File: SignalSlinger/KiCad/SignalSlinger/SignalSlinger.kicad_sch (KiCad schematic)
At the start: 58 parts, among them J101 Conn_01x02, J102 Conn_01x02, J103 Conn_01x02, J104 Conn_01x02, J105 Conn_01x02, J106 Conn_01x02, J107 DB9 Female, J108 Conn_01x02, J109 Conn_01x03, J110 Conn_01x02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

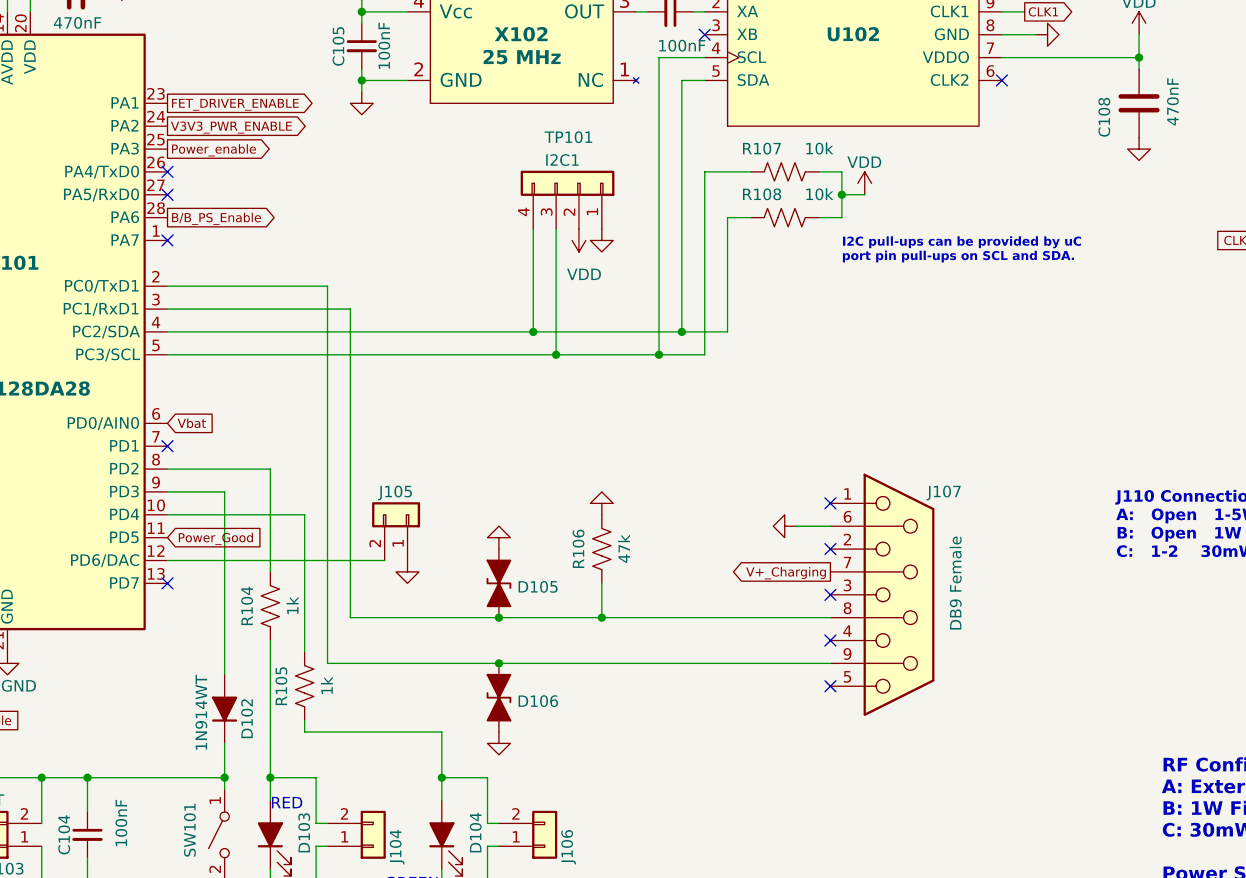
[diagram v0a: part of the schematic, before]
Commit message: KiCad
Added support for straight key and paddles
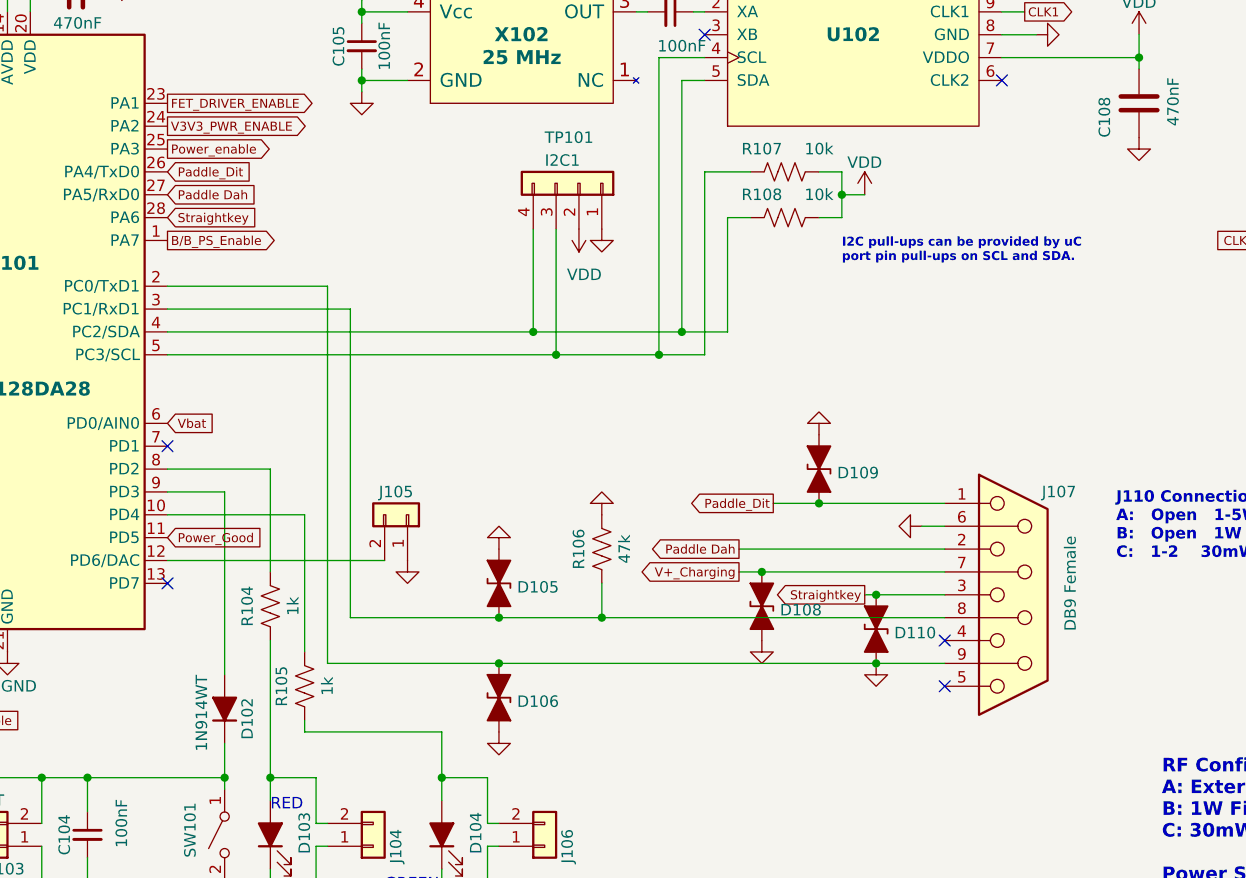
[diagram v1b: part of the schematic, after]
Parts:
- added D108, D109, D110: ESD9B5.0ST5G_1, Diode_SMD:D_0603_1608Metric, symbol Diode:ESD9B5.0ST5G_1
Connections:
- net B/B_PS_Enable: now also U101.1 (PA7); no longer U101.28 (PA6)
- net GND: now also D106.1 (A1), J107.9, U101.2 (PC0/TxD1), D108.2 (A2), D109.1 (A1), D110.2 (A2)
- net V+_Charging: now also D108.1 (A1)
- net Paddle_Dit: now reaches U101.26 (PA4/TxD0)
- net Paddle_Dit: now also J107.1, D109.2 (A2)
- net Paddle Dah: now reaches U101.27 (PA5/RxD0)
- net Paddle Dah: now also J107.2
- net Straightkey: now reaches J107.3
- net Straightkey: now also U101.28 (PA6), D110.1 (A1)
- no-connect marks 22 -> 16
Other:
- moved on the sheet: J107

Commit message: Updates
Schematic and PCB updates
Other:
- note removed: "J110 Connections A: Open 1-5W Variable RF Out CW Tx B: Open 1W Fixed RF Out CW Tx C: 1-2 30mW Fixed RF Out CW Tx"
- title: (none) -> SignalSlinger Design
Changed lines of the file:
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@@
 (kicad_sch (version 20211123) (generator eeschema)
   (paper "A4")
+  (title_block
+    (title "SignalSlinger Design")
+    (date "2023-06-20")
+    (rev "1.0")
+  )
   (junction (at 158.75 133.35) (diameter 0) (color 0 0 0 0)
   )
@@
     (effects (font (size 1.27 1.27) (thickness 0.254) bold) (justify left bottom))
   )
-  (text "J110 Connections\nA:   Open   1-5W Variable RF Out CW Tx\nB:   Open   1W Fixed RF Out CW Tx\nC:   1-2    30mW Fixed RF Out CW Tx"
-    (at 185.42 121.92 0)
-    (effects (font (size 1.27 1.27) (thickness 0.254) bold) (justify left bottom))
-  )
   (text "RF Configurations\nA: External 5-12.5V = 1-5W Variable RF Out CW Tx\nB: 1W Fixed RF Out CW Tx\nC: 30mW Fixed RF Out CW Tx\n\nPower Source Configurations\n1. External 5-12.5V\n2. Internal LiIon Battery (3.2-4.2V)\n\n"
     (at 190.5 165.1 0)
@@
       (reference "#PWR0233") (unit 1) (value "GND") (footprint "")
     )
+    (path "/b7c888bf-e50e-45b8-8886-9bc5abf637fe/7e7a61a5-2fd3-45c0-94ac-d31b757fdb9c"
+      (reference "#PWR0234") (unit 1) (value "GND") (footprint "")
+    )
     (path "/da189f43-fd1f-445a-980b-345fda8b9a74/b600cc7c-7732-4f3a-9659-2132a29c4d79"
       (reference "#PWR0301") (unit 1) (value "GND") (footprint "")
@@
       (reference "HDWR412") (unit 1) (value "Pin Header Shorting Jumpers") (footprint "")
     )
+    (path "/5a65e8dc-078c-4a84-92a2-c8664e602338/6dd4c5c1-cbca-4eb3-9be0-3e6afa74ef4c"
+      (reference "HDWR413") (unit 1) (value "FTDI Adapter PCB") (footprint "")
+    )
     (path "/48f385a0-9ac3-46be-bebb-920052f20de4"
       (reference "J101") (unit 1) (value "Conn_01x02") (footprint "Connector_PinSocket_2.54mm:PinSocket_1x02_P2.54mm_Vertical")
@@
       (reference "R204") (unit 1) (value "1M") (footprint "Resistor_SMD:R_0805_2012Metric")
     )
+    (path "/b7c888bf-e50e-45b8-8886-9bc5abf637fe/a604157e-b596-422f-8a01-c3245280c807"
+      (reference "R205") (unit 1) (value "105k") (footprint "Resistor_SMD:R_0805_2012Metric")
+    )
     (path "/8753d621-69e1-4251-a22d-f8eaf42e9c5c"

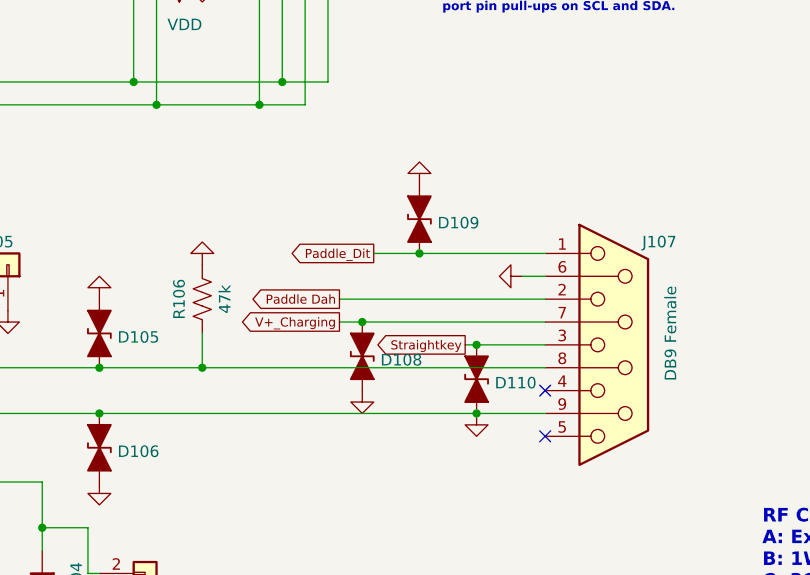
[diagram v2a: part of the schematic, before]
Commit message: Schematic Debug
Fixed misplaced varistor
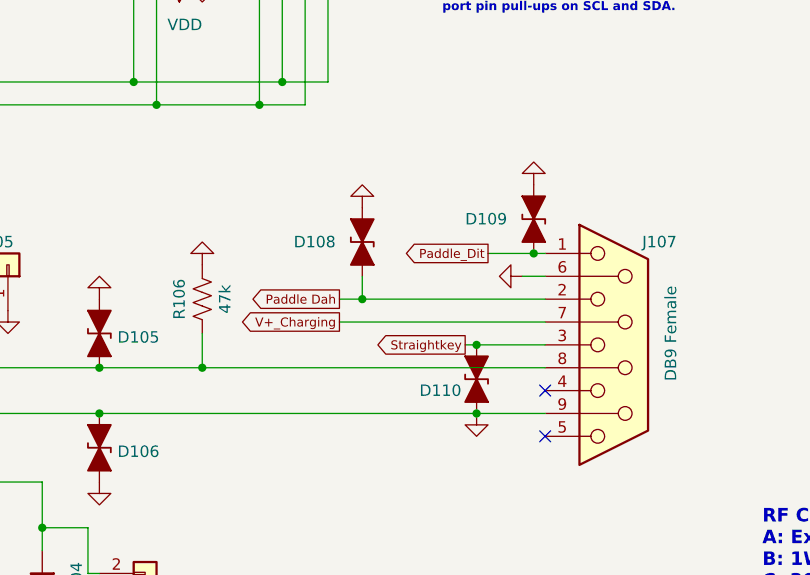
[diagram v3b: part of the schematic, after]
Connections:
- net GND: now also D108.1 (A1); no longer D108.2 (A2)
- net Paddle Dah: now also D108.2 (A2)
- net V+_Charging: no longer D108.1 (A1)
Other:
- moved on the sheet: D108, D109
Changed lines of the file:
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@@
   (junction (at 196.85 40.64) (diameter 0) (color 0 0 0 0)
   )
-  (junction (at 152.4 115.57) (diameter 0) (color 0 0 0 0)
+  (junction (at 146.05 120.65) (diameter 0) (color 0 0 0 0)
+  )
+  (junction (at 165.1 115.57) (diameter 0) (color 0 0 0 0)
   )
   (junction (at 86.36 160.02) (diameter 0) (color 0 0 0 0)
@@
   (junction (at 137.16 96.52) (diameter 0) (color 0 0 0 0)
   )
-  (junction (at 146.05 123.19) (diameter 0) (color 0 0 0 0)
-  )
   (junction (at 128.27 128.27) (diameter 0) (color 0 0 0 0)
   )
@@
     (stroke (width 0) (type default) (color 0 0 0 0))
   )
-  (wire (pts (xy 152.4 115.57) (xy 166.37 115.57))
+  (wire (pts (xy 165.1 115.57) (xy 166.37 115.57))
     (stroke (width 0) (type default) (color 0 0 0 0))
   )
@@
     (stroke (width 0) (type default) (color 0 0 0 0))
   )
-  (wire (pts (xy 143.51 123.19) (xy 146.05 123.19))
+  (wire (pts (xy 143.51 123.19) (xy 166.37 123.19))
     (stroke (width 0) (type default) (color 0 0 0 0))
   )
@@
     (stroke (width 0) (type default) (color 0 0 0 0))
   )
-  (wire (pts (xy 143.51 120.65) (xy 166.37 120.65))
+  (wire (pts (xy 143.51 120.65) (xy 146.05 120.65))
     (stroke (width 0) (type default) (color 0 0 0 0))
   )
@@
     (stroke (width 0) (type default) (color 0 0 0 0))
   )
-  (wire (pts (xy 147.32 115.57) (xy 152.4 115.57))
+  (wire (pts (xy 160.02 115.57) (xy 165.1 115.57))
     (stroke (width 0) (type default) (color 0 0 0 0))
   )
@@
     (stroke (width 0) (type default) (color 0 0 0 0))
   )
-  (wire (pts (xy 146.05 123.19) (xy 166.37 123.19))
+  (wire (pts (xy 146.05 118.11) (xy 146.05 120.65))
     (stroke (width 0) (type default) (color 0 0 0 0))
   )
@@
     (stroke (width 0) (type default) (color 0 0 0 0))
   )
+  (wire (pts (xy 146.05 120.65) (xy 166.37 120.65))
+    (stroke (width 0) (type default) (color 0 0 0 0))
+  )
   (wire (pts (xy 62.23 58.42) (xy 62.23 60.96))
     (stroke (width 0) (type default) (color 0 0 0 0))
@@
     )
   )
-  (global_label "Paddle_Dit" (shape output) (at 147.32 115.57 180) (fields_autoplaced)
+  (global_label "Paddle_Dit" (shape output) (at 160.02 115.57 180) (fields_autoplaced)
     (effects (font (size 1 1)) (justify right))
-    (property "Intersheet References" "${INTERSHEET_REFS}" (id 0) (at 137.5152 115.5075 0)
+    (property "Intersheet References" "${INTERSHEET_REFS}" (id 0) (at 150.2152 115.5075 0)
       (effects (font (size 1 1)) (justify right) hide)
     )
@@
     (pin "4")
   )
-  (symbol (lib_id "power:GND") (at 152.4 107.95 0) (mirror x) (unit 1)
+  (symbol (lib_id "power:GND") (at 165.1 107.95 0) (mirror x) (unit 1)
     (in_bom yes) (on_board yes) (fields_autoplaced)
-    (property "Reference" "#PWR0157" (id 0) (at 152.4 101.6 0)
+    (property "Reference" "#PWR0157" (id 0) (at 165.1 101.6 0)
       (effects (font (size 1.27 1.27)) hide)
     )
-    (property "Value" "GND" (id 1) (at 152.4 103.5066 0)
+    (property "Value" "GND" (id 1) (at 165.1 103.5066 0)
       (effects (font (size 1.27 1.27)) hide)
     )
-    (property "Footprint" "" (id 2) (at 152.4 107.95 0)
+    (property "Footprint" "" (id 2) (at 165.1 107.95 0)
       (effects (font (size 1.27 1.27)) hide)
     )
-    (property "Datasheet" "" (id 3) (at 152.4 107.95 0)
+    (property "Datasheet" "" (id 3) (at 165.1 107.95 0)
       (effects (font (size 1.27 1.27)) hide)
     )
@@
     (pin "2")
   )
-  (symbol (lib_id "Diode:ESD9B5.0ST5G_1") (at 146.05 127 270) (unit 1)
-    (in_bom yes) (on_board yes) (fields_autoplaced)
-    (property "Reference" "D108" (id 0) (at 148.0566 127.4338 90)
+  (symbol (lib_id "Diode:ESD9B5.0ST5G_1") (at 146.05 114.3 270) (unit 1)
+    (in_bom yes) (on_board yes)
+    (property "Reference" "D108" (id 0) (at 138.43 114.3 90)
       (effects (font (size 1.27 1.27)) (justify left))
     )
-    (property "Value" "ESD9B5.0ST5G_1" (id 1) (at 144.907 129.0066 90)
+    (property "Value" "ESD9B5.0ST5G_1" (id 1) (at 144.907 116.3066 90)
       (effects (font (size 1.27 1.27)) (justify right) hide)
     )
-    (property "Footprint" "Diode_SMD:D_0603_1608Metric" (id 2) (at 146.05 127 0)
+    (property "Footprint" "Diode_SMD:D_0603_1608Metric" (id 2) (at 146.05 114.3 0)
       (effects (font (size 1.27 1.27)) hide)
     )
-    (property "Datasheet" "" (id 3) (at 146.05 127 0)
+    (property "Datasheet" "" (id 3) (at 146.05 114.3 0)
       (effects (font (size 1.27 1.27)) hide)
     )
-    (property "Digi-Key Part No." "CG0603MLC-05LECT-ND" (id 4) (at 146.05 127 0)
+    (property "Digi-Key Part No." "CG0603MLC-05LECT-ND" (id 4) (at 146.05 114.3 0)
       (effects (font (size 1.27 1.27)) hide)
     )
-    (property "Link" "<a href=\"https://www.digikey.com/products/en?keywords=CG0603MLC-05LECT-ND\">Link</a>" (id 5) (at 146.05 127 0)
+    (property "Link" "<a href=\"https://www.digikey.com/products/en?keywords=CG0603MLC-05LECT-ND\">Link</a>" (id 5) (at 146.05 114.3 0)
       (effects (font (size 1.27 1.27)) hide)
     )
-    (property "Manufacturer" "Bourns Inc." (id 6) (at 146.05 127 0)
+    (property "Manufacturer" "Bourns Inc." (id 6) (at 146.05 114.3 0)
       (effects (font (size 1.27 1.27)) hide)
     )
-    (property "Manufacturer PN" "CG0603MLC-05LE" (id 7) (at 146.05 127 0)
+    (property "Manufacturer PN" "CG0603MLC-05LE" (id 7) (at 146.05 114.3 0)
       (effects (font (size 1.27 1.27)) hide)
     )
-    (property "Description" "VARISTOR 0603" (id 8) (at 146.05 127 0)
+    (property "Description" "VARISTOR 0603" (id 8) (at 146.05 114.3 0)
       (effects (font (size 1.27 1.27)) hide)
     )
-    (property "LCSC Part Number" "C316054" (id 9) (at 146.05 127 0)
+    (property "LCSC Part Number" "C316054" (id 9) (at 146.05 114.3 0)
       (effects (font (size 1.27 1.27)) hide)
     )
@@
     (pin "2")
   )
-  (symbol (lib_id "power:GND") (at 146.05 130.81 0) (unit 1)
+  (symbol (lib_id "power:GND") (at 146.05 110.49 0) (mirror x) (unit 1)
     (in_bom yes) (on_board yes) (fields_autoplaced)
-    (property "Reference" "#PWR0156" (id 0) (at 146.05 137.16 0)
+    (property "Reference" "#PWR0156" (id 0) (at 146.05 104.14 0)
       (effects (font (size 1.27 1.27)) hide)
     )
-    (property "Value" "GND" (id 1) (at 146.05 135.2534 0)
+    (property "Value" "GND" (id 1) (at 146.05 106.0466 0)
       (effects (font (size 1.27 1.27)) hide)
     )
-    (property "Footprint" "" (id 2) (at 146.05 130.81 0)
+    (property "Footprint" "" (id 2) (at 146.05 110.49 0)
       (effects (font (size 1.27 1.27)) hide)
     )
-    (property "Datasheet" "" (id 3) (at 146.05 130.81 0)
+    (property "Datasheet" "" (id 3) (at 146.05 110.49 0)
       (effects (font (size 1.27 1.27)) hide)
     )
@@
   )
   (symbol (lib_id "Diode:ESD9B5.0ST5G_1") (at 158.75 129.54 270) (unit 1)
-    (in_bom yes) (on_board yes) (fields_autoplaced)
-    (property "Reference" "D110" (id 0) (at 160.7566 129.9738 90)
+    (in_bom yes) (on_board yes)
+    (property "Reference" "D110" (id 0) (at 152.4 130.81 90)
       (effects (font (size 1.27 1.27)) (justify left))
     )
@@
     (pin "1")
   )
-  (symbol (lib_id "Diode:ESD9B5.0ST5G_1") (at 152.4 111.76 270) (unit 1)
-    (in_bom yes) (on_board yes) (fields_autoplaced)
-    (property "Reference" "D109" (id 0) (at 154.4066 112.1938 90)
+  (symbol (lib_id "Diode:ESD9B5.0ST5G_1") (at 165.1 111.76 270) (unit 1)
+    (in_bom yes) (on_board yes)
+    (property "Reference" "D109" (id 0) (at 157.48 111.76 90)
       (effects (font (size 1.27 1.27)) (justify left))
     )
-    (property "Value" "ESD9B5.0ST5G_1" (id 1) (at 151.257 113.7666 90)
+    (property "Value" "ESD9B5.0ST5G_1" (id 1) (at 163.957 113.7666 90)
       (effects (font (size 1.27 1.27)) (justify right) hide)
     )
-    (property "Footprint" "Diode_SMD:D_0603_1608Metric" (id 2) (at 152.4 111.76 0)
+    (property "Footprint" "Diode_SMD:D_0603_1608Metric" (id 2) (at 165.1 111.76 0)
       (effects (font (size 1.27 1.27)) hide)
     )
-    (property "Datasheet" "" (id 3) (at 152.4 111.76 0)
+    (property "Datasheet" "" (id 3) (at 165.1 111.76 0)
       (effects (font (size 1.27 1.27)) hide)
     )
-    (property "Digi-Key Part No." "CG0603MLC-05LECT-ND" (id 4) (at 152.4 111.76 0)
+    (property "Digi-Key Part No." "CG0603MLC-05LECT-ND" (id 4) (at 165.1 111.76 0)
       (effects (font (size 1.27 1.27)) hide)
     )
-    (property "Link" "<a href=\"https://www.digikey.com/products/en?keywords=CG0603MLC-05LECT-ND\">Link</a>" (id 5) (at 152.4 111.76 0)
+    (property "Link" "<a href=\"https://www.digikey.com/products/en?keywords=CG0603MLC-05LECT-ND\">Link</a>" (id 5) (at 165.1 111.76 0)
       (effects (font (size 1.27 1.27)) hide)
     )
-    (property "Manufacturer" "Bourns Inc." (id 6) (at 152.4 111.76 0)
+    (property "Manufacturer" "Bourns Inc." (id 6) (at 165.1 111.76 0)
       (effects (font (size 1.27 1.27)) hide)
     )
-    (property "Manufacturer PN" "CG0603MLC-05LE" (id 7) (at 152.4 111.76 0)
+    (property "Manufacturer PN" "CG0603MLC-05LE" (id 7) (at 165.1 111.76 0)
       (effects (font (size 1.27 1.27)) hide)
     )
-    (property "Description" "VARISTOR 0603" (id 8) (at 152.4 111.76 0)
+    (property "Description" "VARISTOR 0603" (id 8) (at 165.1 111.76 0)
       (effects (font (size 1.27 1.27)) hide)
     )
-    (property "LCSC Part Number" "C316054" (id 9) (at 152.4 111.76 0)
+    (property "LCSC Part Number" "C316054" (id 9) (at 165.1 111.76 0)
       (effects (font (size 1.27 1.27)) hide)
     )
